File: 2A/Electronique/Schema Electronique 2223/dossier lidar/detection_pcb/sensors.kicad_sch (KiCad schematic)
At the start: 64 parts, among them U1 VL53L1X_module, U10 VL53L1X_module, U11 VL53L1X_module, U12 VL53L1X_module, U13 VL53L1X_module, U14 VL53L1X_module, U15 VL53L1X_module, U16 VL53L1X_module, U2 VL53L1X_module, U3 VL53L1X_module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

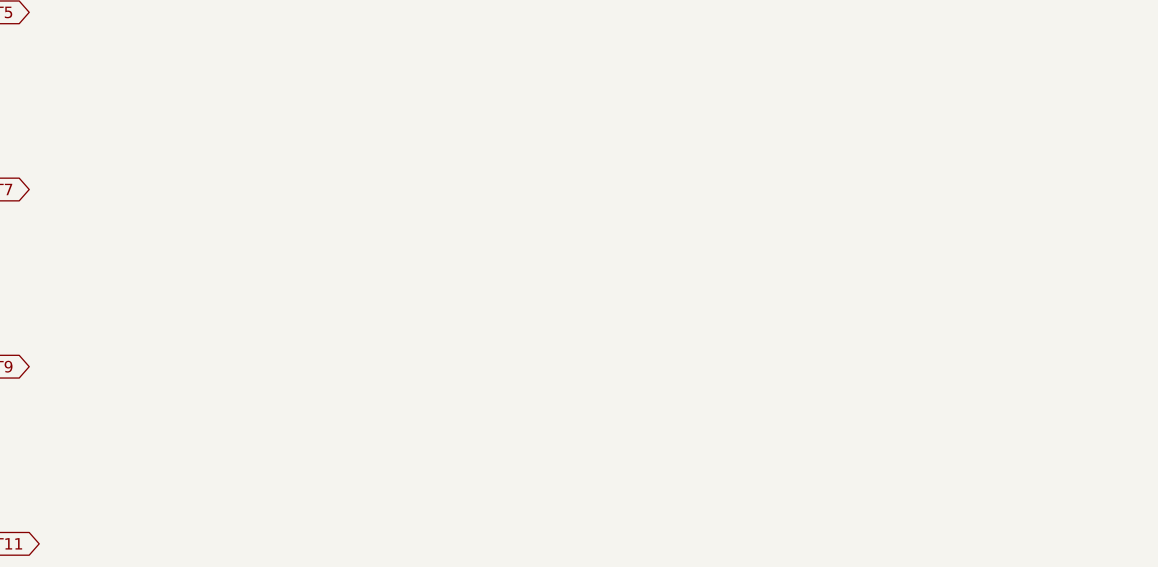
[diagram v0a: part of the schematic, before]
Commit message: removed duplicated project, updated schematic and pcb, added BOM
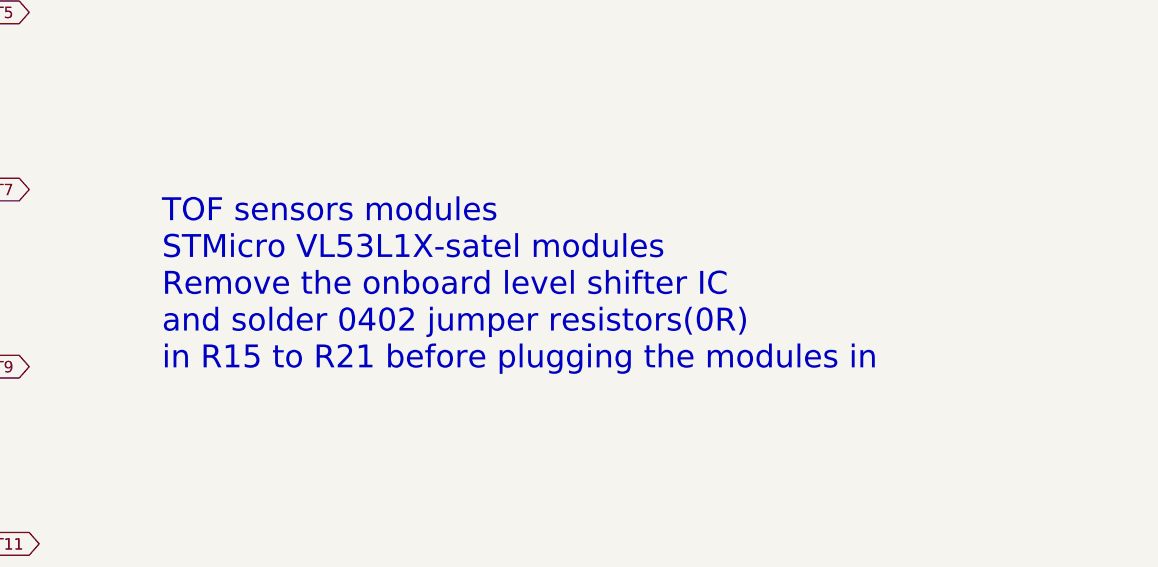
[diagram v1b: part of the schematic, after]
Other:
- note added: "TOF sensors modules STMicro VL53L1X-satel modules Remove the onboard level shifter IC and solder 0402 jumper resistors(0R) in R15 to R21 before plugging the modules in"
